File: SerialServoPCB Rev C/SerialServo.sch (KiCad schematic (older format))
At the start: 49 parts, among them J1 Conn_01x04, J2 Conn_01x06, J3 Conn_01x05, J4 Conn_01x03, J5 Conn_01x03, J6 Conn_01x03, J8 Conn_01x02, SW1 SW_Push, SW2 SW_Push, U1 PIC16F1847-ISO, U2 LM358A

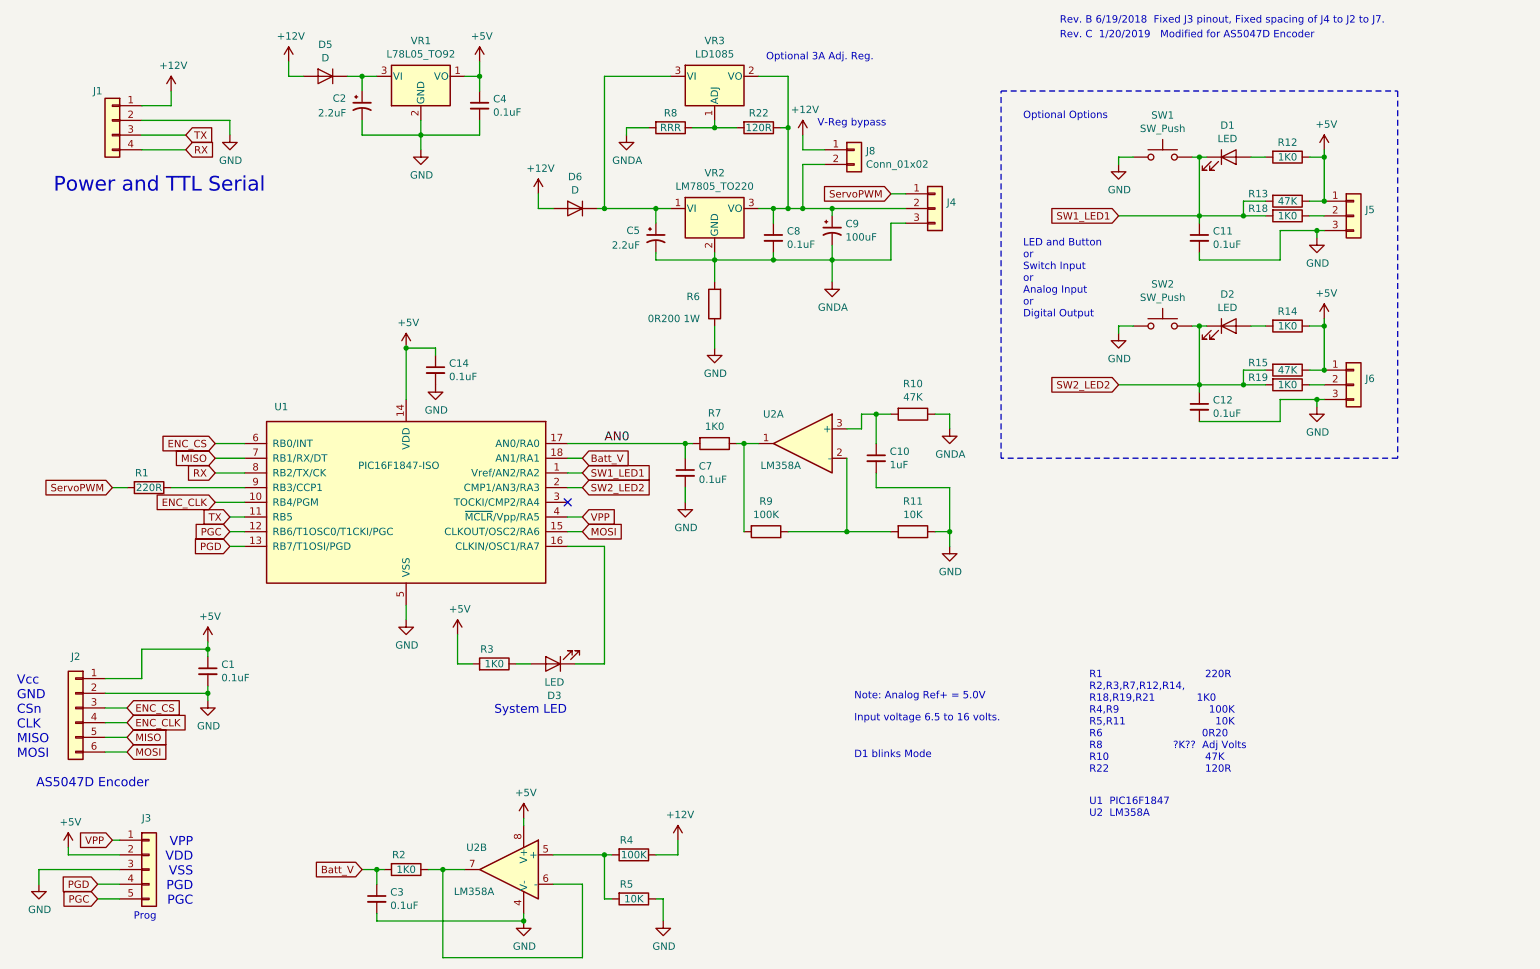
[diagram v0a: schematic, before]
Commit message: New Rev C works
except for the bootloader
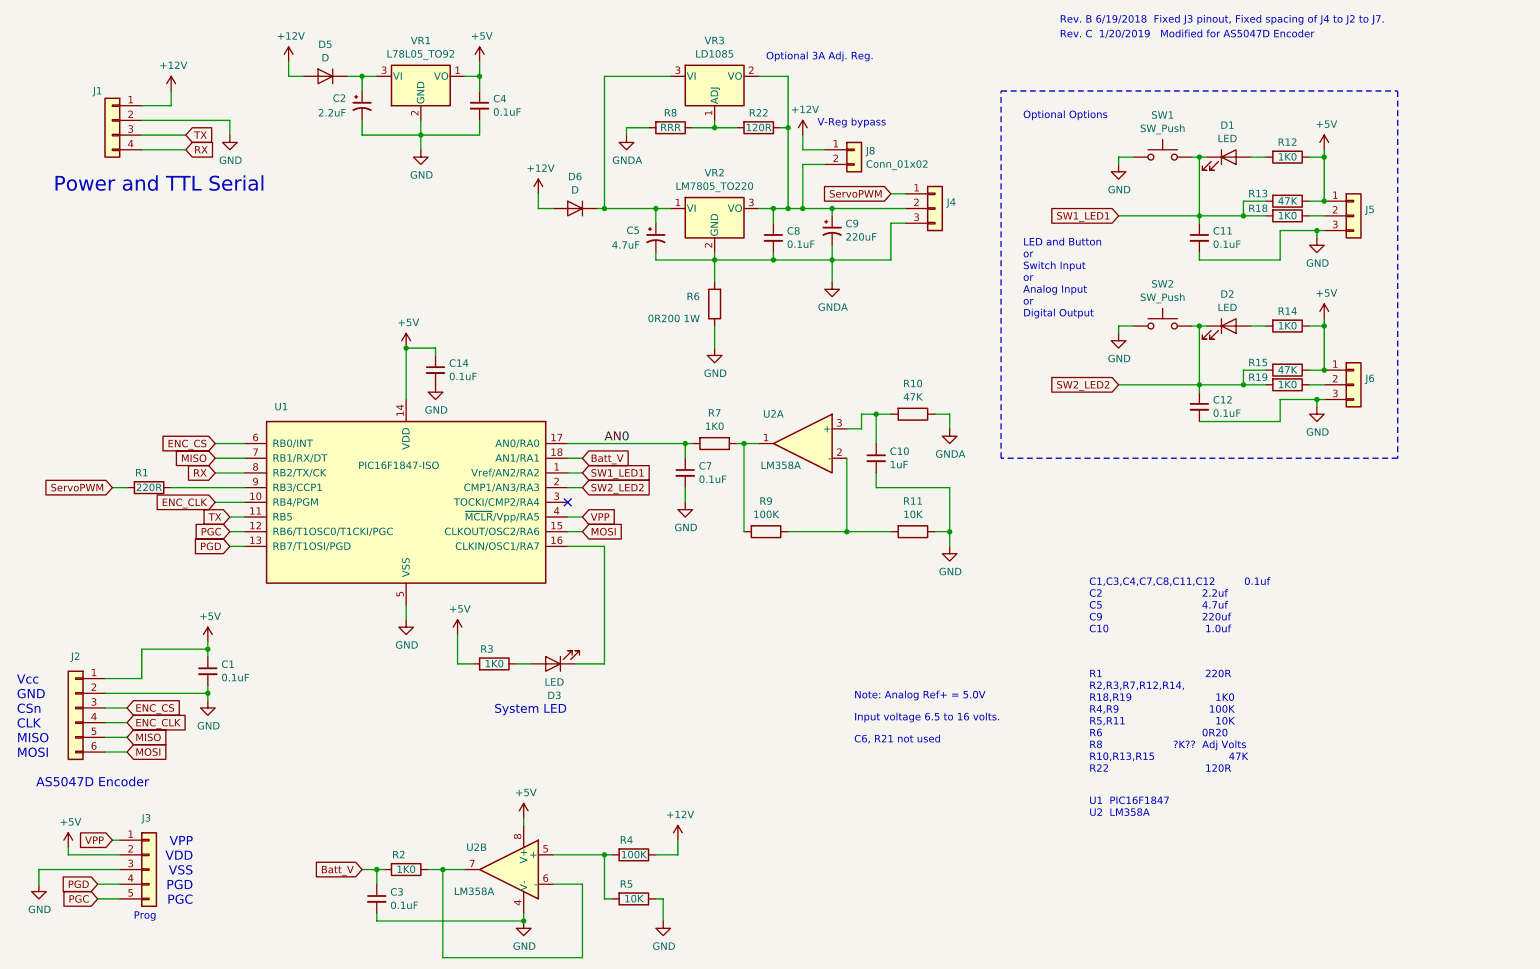
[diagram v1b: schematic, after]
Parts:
- C5: value 2.2uF -> 4.7uF
- C9: value 100uF -> 220uF
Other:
- note added: "C1,C3,C4,C7,C8,C11,C12 0.1uf\nC2 2.2uf\nC5 4.7uf\nC9 220uf\nC10 1.0uf"
- note added: "C6, R21 not used"
- note added: "R1 220R\nR2,R3,R7,R12,R14,\nR18,R19 1K0\nR4,R9 100K\nR5,R11 10K\nR6 0R20\nR8 ?K?? Adj Volts\nR10,R13,R15 47K\nR22 120R"
- note removed: "D1 blinks Mode"
- note removed: "R1 220R\nR2,R3,R7,R12,R14,\nR18,R19,R21 1K0\nR4,R9 100K\nR5,R11 10K\nR6 0R20\nR8 ?K?? Adj Volts\nR10 47K\nR22 120R"
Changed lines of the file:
@@
 P 6100 2050
 F 0 "C9" H 6191 2096 50  0000 L CNN
-F 1 "100uF" H 6191 2005 50  0000 L CNN
+F 1 "220uF" H 6191 2005 50  0000 L CNN
 F 2 "Capacitor_THT:CP_Radial_D8.0mm_P5.00mm" H 6100 2050 50  0001 C CNN
 F 3 "~" H 6100 2050 50  0001 C CNN
@@
 P 4900 2100
 F 0 "C5" H 4700 2150 50  0000 L CNN
-F 1 "2.2uF" H 4600 2050 50  0000 L CNN
+F 1 "4.7uF" H 4600 2050 50  0000 L CNN
 F 2 "Capacitor_THT:CP_Radial_D5.0mm_P2.00mm" H 4900 2100 50  0001 C CNN
 F 3 "~" H 4900 2100 50  0001 C CNN
@@
 Wire Wire Line
 	900  6300 1250 6300
-Text Notes 7850 5750 0    50   ~ 0
-R1                                220R\nR2,R3,R7,R12,R14,\nR18,R19,R21             1K0\nR4,R9                            100K\nR5,R11                            10K\nR6                               0R20\nR8                      ?K??  Adj Volts\nR10                              47K\nR22                              120R
 Text Notes 7850 6050 0    50   ~ 0
 U1  PIC16F1847\nU2  LM358A\n
 Text Notes 7650 650  0    50   ~ 0
 Rev. B 6/19/2018  Fixed J3 pinout, Fixed spacing of J4 to J2 to J7.
-Text Notes 6250 5650 0    50   ~ 0
-D1 blinks Mode
 Text Notes 7400 1300 0    50   ~ 0
 Optional Options
@@
 Wire Notes Line
 	7250 3600 7250 1100
+Text Notes 6250 5550 0    50   ~ 0
+C6, R21 not used
+Text Notes 7850 4800 0    50   ~ 0
+C1,C3,C4,C7,C8,C11,C12         0.1uf\nC2                               2.2uf\nC5                               4.7uf\nC9                               220uf\nC10                              1.0uf
+Text Notes 7850 5750 0    50   ~ 0
+R1                                220R\nR2,R3,R7,R12,R14,\nR18,R19                          1K0\nR4,R9                            100K\nR5,R11                            10K\nR6                               0R20\nR8                      ?K??  Adj Volts\nR10,R13,R15                       47K\nR22                              120R
 $EndSCHEMATC
